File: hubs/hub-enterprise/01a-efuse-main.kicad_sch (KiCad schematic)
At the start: 11 parts, among them J101 CEC_PWR_IN_2P, U101 TPS25940LRVCR

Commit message: WIP snapshot: composition agent iterating (durability)
Co-Authored-By: Claude Fable 5 <noreply@anthropic.com>
Claude-Session: https://claude.ai/code/session_011q5bmwF5BFtSf8Ft5vT1DZ
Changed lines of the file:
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@@
 	(wire (pts (xy 177.8 107.95) (xy 196.85 107.95))
 		(stroke (width 0) (type default)))
-	(wire (pts (xy 64.77 133.35) (xy 64.77 143.51))
+	(wire (pts (xy 64.77 138.43) (xy 64.77 148.59))
 		(stroke (width 0) (type default)))
-	(wire (pts (xy 80.01 133.35) (xy 80.01 143.51))
+	(wire (pts (xy 80.01 138.43) (xy 80.01 148.59))
 		(stroke (width 0) (type default)))
 	(junction (at 97.79 67.31) (diameter 0) (color 0 0 0 0))
@@
 	(symbol
 		(lib_id "cec-power:+5V_MAIN")
-		(at 64.77 133.35 180)
-		(unit 1)
-		(exclude_from_sim no)
-		(in_bom yes)
-		(on_board yes)
-		(dnp no)
-		(property "Reference" "#PWR110" (at 64.77 130.81 0) (effects (font (size 1.27 1.27)) (hide yes)))
-		(property "Value" "+5V_MAIN" (at 64.77 139.7 0) (effects (font (size 1.27 1.27))))
+		(at 64.77 138.43 180)
+		(unit 1)
+		(exclude_from_sim no)
+		(in_bom yes)
+		(on_board yes)
+		(dnp no)
+		(property "Reference" "#PWR110" (at 64.77 135.89 0) (effects (font (size 1.27 1.27)) (hide yes)))
+		(property "Value" "+5V_MAIN" (at 64.77 144.78 0) (effects (font (size 1.27 1.27))))
 		(pin "1")
 		(instances
@@
 	(symbol
 		(lib_id "cec-power:PWR_FLAG")
-		(at 64.77 143.51 0)
-		(unit 1)
-		(exclude_from_sim no)
-		(in_bom yes)
-		(on_board yes)
-		(dnp no)
-		(property "Reference" "#FLG111" (at 64.77 140.97 0) (effects (font (size 1.27 1.27)) (hide yes)))
-		(property "Value" "PWR_FLAG" (at 64.77 135.89 0) (effects (font (size 1.27 1.27))))
+		(at 64.77 148.59 0)
+		(unit 1)
+		(exclude_from_sim no)
+		(in_bom yes)
+		(on_board yes)
+		(dnp no)
+		(property "Reference" "#FLG111" (at 64.77 146.05 0) (effects (font (size 1.27 1.27)) (hide yes)))
+		(property "Value" "PWR_FLAG" (at 64.77 140.97 0) (effects (font (size 1.27 1.27))))
 		(pin "1")
 		(instances
@@
 	(symbol
 		(lib_id "cec-power:PWR_FLAG")
-		(at 80.01 133.35 180)
-		(unit 1)
-		(exclude_from_sim no)
-		(in_bom yes)
-		(on_board yes)
-		(dnp no)
-		(property "Reference" "#FLG112" (at 80.01 130.81 0) (effects (font (size 1.27 1.27)) (hide yes)))
-		(property "Value" "PWR_FLAG" (at 80.01 138.43 0) (effects (font (size 1.27 1.27))))
+		(at 80.01 138.43 180)
+		(unit 1)
+		(exclude_from_sim no)
+		(in_bom yes)
+		(on_board yes)
+		(dnp no)
+		(property "Reference" "#FLG112" (at 80.01 135.89 0) (effects (font (size 1.27 1.27)) (hide yes)))
+		(property "Value" "PWR_FLAG" (at 80.01 143.51 0) (effects (font (size 1.27 1.27))))
 		(pin "1")
 		(instances
@@
 	(symbol
 		(lib_id "cec-power:GND")
-		(at 80.01 143.51 0)
-		(unit 1)
-		(exclude_from_sim no)
-		(in_bom yes)
-		(on_board yes)
-		(dnp no)
-		(property "Reference" "#PWR113" (at 80.01 140.97 0) (effects (font (size 1.27 1.27)) (hide yes)))
-		(property "Value" "GND" (at 80.01 148.59 0) (effects (font (size 1.27 1.27))))
-		(pin "1")
-		(instances
+		(at 80.01 148.59 0)
+		(unit 1)
+		(exclude_from_sim no)
+		(in_bom yes)
+		(on_board yes)
+		(dnp no)
+		(property "Reference" "#PWR113" (at 80.01 146.05 0) (effects (font (size 1.27 1.27)) (hide yes)))
+		(property "Value" "GND" (at 80.01 153.67 0) (effects (font (size 1.27 1.27))))
+		(pin "1")
+		(instances

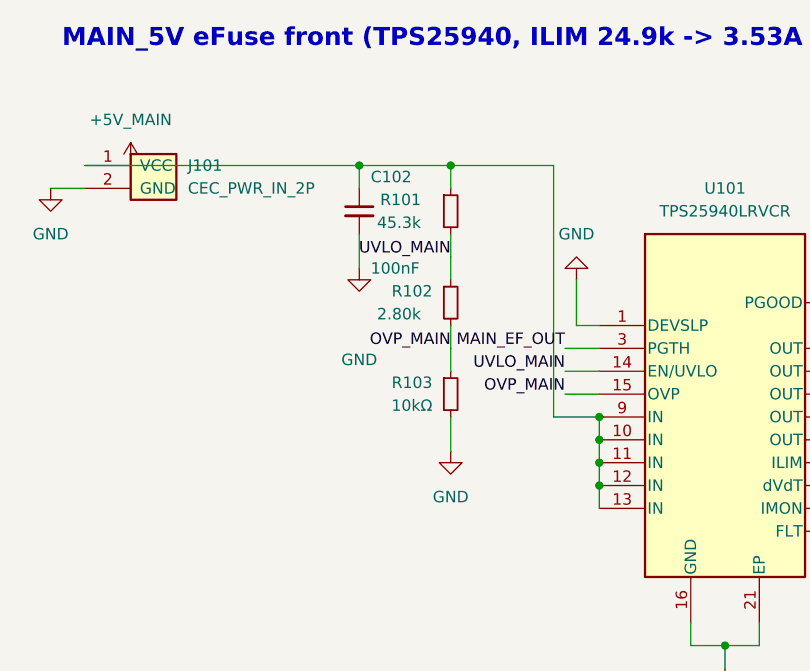
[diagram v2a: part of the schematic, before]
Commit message: Standard-tier synthesis: beta-line plan + 11-item owner decision list
Synthesis of the six-report review pass (SYNTHESIS-beta-plan.md):
measured fleet-reality table (Hub nearest to sellable but CI-red on the
shared USB-C footprint defect found on three boards; 12VHPWR near with
one genuinely shipped defect — the never-fixed U4/U3 REF thermal
coupling; the MANDATORY 24-pin is the critical path with a live rev2
erratum and a DETECT placeholder in the reference schematic; EPS and
both PCIe boards are placement-only with zero copper despite docs
claiming otherwise — stale in our favor on C6/FTP). Eight-item
no-decision hygiene wave (W1-W8) ready to run under the beta flag;
eleven deduped owner decisions (D-1..D-11) led by kit/cable SKUs that
don't exist, the 24-pin rev3a-vs-full-respin scope call, and SKU
collapse options (single PCIe board, EPS-1 population). Owner-queue row
updated to point at the D-list.

Co-Authored-By: Claude Fable 5 <noreply@anthropic.com>
Claude-Session: https://claude.ai/code/session_011q5bmwF5BFtSf8Ft5vT1DZ
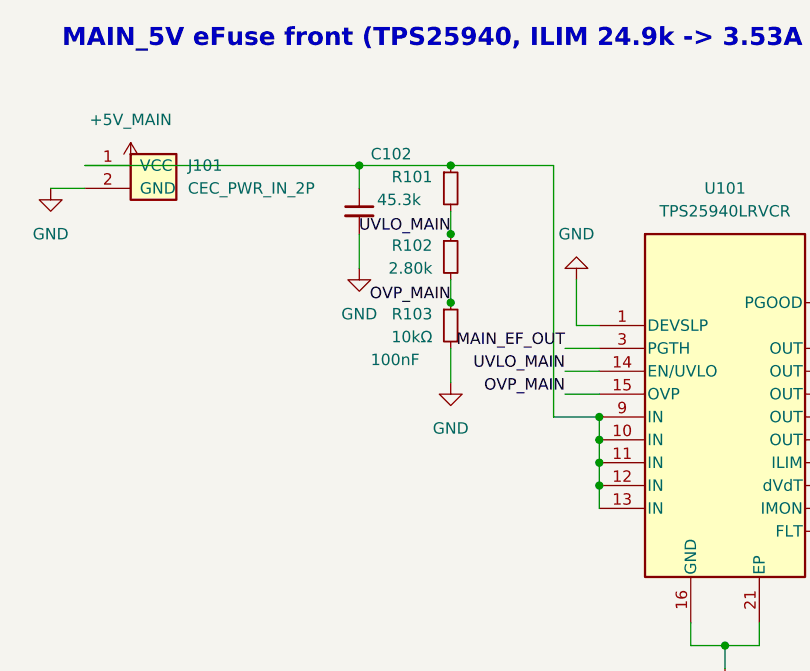
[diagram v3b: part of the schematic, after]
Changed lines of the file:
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@@
 	(symbol
 		(lib_id "cec-vendor:R_Small")
-		(at 113.03 72.39 0)
-		(unit 1)
-		(exclude_from_sim no)
-		(in_bom yes)
-		(on_board yes)
-		(dnp no)
-		(fields_autoplaced yes)
-		(property "Reference" "R101" (at 109.728 71.12 0) (effects (font (size 1.27 1.27)) (justify right)))
-		(property "Value" "45.3k" (at 109.728 73.66 0) (effects (font (size 1.27 1.27)) (justify right)))
-		(property "Footprint" "cec-Resistor_SMD:R_0402_1005Metric" (at 113.03 72.39 0) (effects (font (size 1.27 1.27)) (hide yes)))
-		(property "Datasheet" "" (at 113.03 72.39 0) (effects (font (size 1.27 1.27)) (hide yes)))
-		(property "Manufacturer" "UNI-ROYAL" (at 113.03 72.39 0) (effects (font (size 1.27 1.27)) (hide yes)))
-		(property "MPN" "0402WGF4532TCE" (at 113.03 72.39 0) (effects (font (size 1.27 1.27)) (hide yes)))
-		(property "Description" "UVLO/OVLO divider top, MAIN_5V eFuse" (at 113.03 72.39 0) (effects (font (size 1.27 1.27)) (hide yes)))
+		(at 113.03 69.85 0)
+		(unit 1)
+		(exclude_from_sim no)
+		(in_bom yes)
+		(on_board yes)
+		(dnp no)
+		(fields_autoplaced yes)
+		(property "Reference" "R101" (at 110.998 68.58 0) (effects (font (size 1.27 1.27)) (justify right)))
+		(property "Value" "45.3k" (at 109.728 71.12 0) (effects (font (size 1.27 1.27)) (justify right)))
+		(property "Footprint" "cec-Resistor_SMD:R_0402_1005Metric" (at 113.03 69.85 0) (effects (font (size 1.27 1.27)) (hide yes)))
+		(property "Datasheet" "" (at 113.03 69.85 0) (effects (font (size 1.27 1.27)) (hide yes)))
+		(property "Manufacturer" "UNI-ROYAL" (at 113.03 69.85 0) (effects (font (size 1.27 1.27)) (hide yes)))
+		(property "MPN" "0402WGF4532TCE" (at 113.03 69.85 0) (effects (font (size 1.27 1.27)) (hide yes)))
+		(property "Description" "UVLO/OVLO divider top, MAIN_5V eFuse" (at 113.03 69.85 0) (effects (font (size 1.27 1.27)) (hide yes)))
 		(pin "1")
 		(pin "2")
@@
 	(symbol
 		(lib_id "cec-vendor:R_Small")
-		(at 113.03 82.55 0)
-		(unit 1)
-		(exclude_from_sim no)
-		(in_bom yes)
-		(on_board yes)
-		(dnp no)
-		(fields_autoplaced yes)
-		(property "Reference" "R102" (at 110.998 81.28 0) (effects (font (size 1.27 1.27)) (justify right)))
-		(property "Value" "2.80k" (at 109.728 83.82 0) (effects (font (size 1.27 1.27)) (justify right)))
-		(property "Footprint" "cec-Resistor_SMD:R_0402_1005Metric" (at 113.03 82.55 0) (effects (font (size 1.27 1.27)) (hide yes)))
-		(property "Datasheet" "" (at 113.03 82.55 0) (effects (font (size 1.27 1.27)) (hide yes)))
-		(property "Manufacturer" "UNI-ROYAL" (at 113.03 82.55 0) (effects (font (size 1.27 1.27)) (hide yes)))
-		(property "MPN" "0402WGF2801TCE" (at 113.03 82.55 0) (effects (font (size 1.27 1.27)) (hide yes)))
-		(property "Description" "UVLO/OVLO divider mid, MAIN_5V eFuse" (at 113.03 82.55 0) (effects (font (size 1.27 1.27)) (hide yes)))
+		(at 113.03 77.47 0)
+		(unit 1)
+		(exclude_from_sim no)
+		(in_bom yes)
+		(on_board yes)
+		(dnp no)
+		(fields_autoplaced yes)
+		(property "Reference" "R102" (at 110.998 76.2 0) (effects (font (size 1.27 1.27)) (justify right)))
+		(property "Value" "2.80k" (at 110.998 78.74 0) (effects (font (size 1.27 1.27)) (justify right)))
+		(property "Footprint" "cec-Resistor_SMD:R_0402_1005Metric" (at 113.03 77.47 0) (effects (font (size 1.27 1.27)) (hide yes)))
+		(property "Datasheet" "" (at 113.03 77.47 0) (effects (font (size 1.27 1.27)) (hide yes)))
+		(property "Manufacturer" "UNI-ROYAL" (at 113.03 77.47 0) (effects (font (size 1.27 1.27)) (hide yes)))
+		(property "MPN" "0402WGF2801TCE" (at 113.03 77.47 0) (effects (font (size 1.27 1.27)) (hide yes)))
+		(property "Description" "UVLO/OVLO divider mid, MAIN_5V eFuse" (at 113.03 77.47 0) (effects (font (size 1.27 1.27)) (hide yes)))
 		(pin "1")
 		(pin "2")
@@
 	(symbol
 		(lib_id "cec-vendor:R_Small")
-		(at 113.03 92.71 0)
-		(unit 1)
-		(exclude_from_sim no)
-		(in_bom yes)
-		(on_board yes)
-		(dnp no)
-		(fields_autoplaced yes)
-		(property "Reference" "R103" (at 110.998 91.44 0) (effects (font (size 1.27 1.27)) (justify right)))
-		(property "Value" "10kΩ" (at 110.998 93.98 0) (effects (font (size 1.27 1.27)) (justify right)))
-		(property "Footprint" "cec-Resistor_SMD:R_0402_1005Metric" (at 113.03 92.71 0) (effects (font (size 1.27 1.27)) (hide yes)))
-		(property "Datasheet" "" (at 113.03 92.71 0) (effects (font (size 1.27 1.27)) (hide yes)))
-		(property "Manufacturer" "UNI-ROYAL" (at 113.03 92.71 0) (effects (font (size 1.27 1.27)) (hide yes)))
-		(property "MPN" "0402WGF1002TCE" (at 113.03 92.71 0) (effects (font (size 1.27 1.27)) (hide yes)))
-		(property "LCSC" "C25744" (at 113.03 92.71 0) (effects (font (size 1.27 1.27)) (hide yes)))
-		(property "Description" "UVLO/OVLO divider bottom, MAIN_5V eFuse" (at 113.03 92.71 0) (effects (font (size 1.27 1.27)) (hide yes)))
+		(at 113.03 85.09 0)
+		(unit 1)
+		(exclude_from_sim no)
+		(in_bom yes)
+		(on_board yes)
+		(dnp no)
+		(fields_autoplaced yes)
+		(property "Reference" "R103" (at 110.998 83.82 0) (effects (font (size 1.27 1.27)) (justify right)))
+		(property "Value" "10kΩ" (at 110.998 86.36 0) (effects (font (size 1.27 1.27)) (justify right)))
+		(property "Footprint" "cec-Resistor_SMD:R_0402_1005Metric" (at 113.03 85.09 0) (effects (font (size 1.27 1.27)) (hide yes)))
+		(property "Datasheet" "" (at 113.03 85.09 0) (effects (font (size 1.27 1.27)) (hide yes)))
+		(property "Manufacturer" "UNI-ROYAL" (at 113.03 85.09 0) (effects (font (size 1.27 1.27)) (hide yes)))
+		(property "MPN" "0402WGF1002TCE" (at 113.03 85.09 0) (effects (font (size 1.27 1.27)) (hide yes)))
+		(property "LCSC" "C25744" (at 113.03 85.09 0) (effects (font (size 1.27 1.27)) (hide yes)))
+		(property "Description" "UVLO/OVLO divider bottom, MAIN_5V eFuse" (at 113.03 85.09 0) (effects (font (size 1.27 1.27)) (hide yes)))
 		(pin "1")
 		(pin "2")
@@
 		(dnp no)
 		(fields_autoplaced yes)
-		(property "Reference" "C102" (at 104.14 68.58 0) (effects (font (size 1.27 1.27)) (justify left)))
-		(property "Value" "100nF" (at 104.14 78.74 0) (effects (font (size 1.27 1.27)) (justify left)))
+		(property "Reference" "C102" (at 104.14 66.04 0) (effects (font (size 1.27 1.27)) (justify left)))
+		(property "Value" "100nF" (at 104.14 88.9 0) (effects (font (size 1.27 1.27)) (justify left)))
 		(property "Footprint" "cec-Capacitor_SMD:C_0402_1005Metric" (at 102.87 72.39 0) (effects (font (size 1.27 1.27)) (hide yes)))
 		(property "Datasheet" "" (at 102.87 72.39 0) (effects (font (size 1.27 1.27)) (hide yes)))
@@
 	(wire (pts (xy 102.87 67.31) (xy 102.87 69.85))
 		(stroke (width 0) (type default)))
-	(wire (pts (xy 113.03 67.31) (xy 113.03 69.85))
-		(stroke (width 0) (type default)))
-	(wire (pts (xy 113.03 74.93) (xy 113.03 77.47))
-		(stroke (width 0) (type default)))
-	(wire (pts (xy 113.03 77.47) (xy 113.03 80.01))
-		(stroke (width 0) (type default)))
-	(wire (pts (xy 113.03 85.09) (xy 113.03 87.63))
-		(stroke (width 0) (type default)))
-	(wire (pts (xy 113.03 87.63) (xy 113.03 90.17))
+	(wire (pts (xy 113.03 72.39) (xy 113.03 74.93))
+		(stroke (width 0) (type default)))
+	(wire (pts (xy 113.03 74.93) (xy 113.03 74.93))
+		(stroke (width 0) (type default)))
+	(wire (pts (xy 113.03 80.01) (xy 113.03 82.55))
+		(stroke (width 0) (type default)))
+	(wire (pts (xy 113.03 82.55) (xy 113.03 82.55))
 		(stroke (width 0) (type default)))
 	(wire (pts (xy 124.46 67.31) (xy 124.46 95.25))
@@
 	(wire (pts (xy 72.39 69.85) (xy 68.58 69.85))
 		(stroke (width 0) (type default)))
-	(wire (pts (xy 113.03 95.25) (xy 113.03 99.06))
+	(wire (pts (xy 113.03 87.63) (xy 113.03 91.44))
 		(stroke (width 0) (type default)))
 	(wire (pts (xy 165.1 115.57) (xy 165.1 119.38))
@@
 	(junction (at 102.87 67.31) (diameter 0) (color 0 0 0 0))
 	(junction (at 113.03 67.31) (diameter 0) (color 0 0 0 0))
+	(junction (at 113.03 74.93) (diameter 0) (color 0 0 0 0))
+	(junction (at 113.03 82.55) (diameter 0) (color 0 0 0 0))
 	(junction (at 129.54 95.25) (diameter 0) (color 0 0 0 0))
 	(junction (at 129.54 97.79) (diameter 0) (color 0 0 0 0))
@@
 	(junction (at 175.26 82.55) (diameter 0) (color 0 0 0 0))
 	(junction (at 175.26 107.95) (diameter 0) (color 0 0 0 0))
-	(label "UVLO_MAIN" (at 113.03 77.47 180) (effects (font (size 1.27 1.27)) (justify right bottom)))
-	(label "OVP_MAIN" (at 113.03 87.63 180) (effects (font (size 1.27 1.27)) (justify right bottom)))
+	(label "UVLO_MAIN" (at 113.03 74.93 180) (effects (font (size 1.27 1.27)) (justify right bottom)))
+	(label "OVP_MAIN" (at 113.03 82.55 180) (effects (font (size 1.27 1.27)) (justify right bottom)))
 	(label "ILIM_MAIN" (at 160.02 100.33 0) (effects (font (size 1.27 1.27)) (justify left bottom)))
 	(label "UVLO_MAIN" (at 125.73 90.17 180) (effects (font (size 1.27 1.27)) (justify right bottom)))
@@
 	(symbol
 		(lib_id "cec-power:GND")
-		(at 113.03 99.06 0)
-		(unit 1)
-		(exclude_from_sim no)
-		(in_bom yes)
-		(on_board yes)
-		(dnp no)
-		(property "Reference" "#PWR105" (at 113.03 96.52 0) (effects (font (size 1.27 1.27)) (hide yes)))
-		(property "Value" "GND" (at 113.03 104.14 0) (effects (font (size 1.27 1.27))))
+		(at 113.03 91.44 0)
+		(unit 1)
+		(exclude_from_sim no)
+		(in_bom yes)
+		(on_board yes)
+		(dnp no)
+		(property "Reference" "#PWR105" (at 113.03 88.9 0) (effects (font (size 1.27 1.27)) (hide yes)))
+		(property "Value" "GND" (at 113.03 96.52 0) (effects (font (size 1.27 1.27))))
 		(pin "1")
 		(instances
@@
 		(dnp no)
 		(property "Reference" "#PWR108" (at 102.87 76.2 0) (effects (font (size 1.27 1.27)) (hide yes)))
-		(property "Value" "GND" (at 102.87 88.9 0) (effects (font (size 1.27 1.27))))
-		(pin "1")
-		(instances
+		(property "Value" "GND" (at 102.87 83.82 0) (effects (font (size 1.27 1.27))))
+		(pin "1")
+		(instances
